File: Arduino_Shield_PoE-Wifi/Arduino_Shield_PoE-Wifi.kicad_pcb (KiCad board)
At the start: 2 copper layers, 100 x 54 mm, 83 parts, among them J1 Conn_02x08, J1 PINHD_2x4_Male, J2 Conn_02x08, J3 PINHD_1x2_Female, J4 PINHD_1x2_Female, SW1 Push_Button, T1 PMV48XP_215, U1 W5500, U2 74HC245, U2 ATECC508A-SSHDA, U3 LMV358IDGK, X2 25MHz 18pF

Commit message: Update
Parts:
- removed A1: ATWINC1500-MR210PB, Wifi_ATWINC1500-MR210PB-ND_Microchip:XCVR_ATWINC1500-MR210PB
- removed C10: 1nF 2KV 1206, PCM_4ms_Capacitor:C_1206
- removed C12, C13: 100nF_0603_16V, PCM_4ms_Capacitor:C_0603
- removed the J1 at (160.8, 137.4)
- removed LED_PB7: Yellow 0805, LED_SMD:LED_0805_2012Metric
- removed RN35, RN36: 1K_0603, PCM_Resistor_SMD_AKL:R_0603_1608Metric
- removed RN53, RN54: 10K_0603, PCM_Resistor_SMD_AKL:R_0603_1608Metric
- removed T1: PMV48XP_215, MOSFET_PMV48XP,215_Nexperia:TO-236_SOT23_NEX
- removed the U2 at (107.6, 167.3)
- removed the U2 at (190.5, 147.7)
- added C7: 10nF_0603_16V, PCM_4ms_Capacitor:C_0603, F.Cu at (200.5, 93.5)
- added C8: 1nF 2KV 1206, PCM_4ms_Capacitor:C_1206, F.Cu at (207.6, 110.0)
- added Cp3: 10uF_25V, Capacitor_THT:CP_Radial_D5.0mm_P2.00mm, F.Cu at (184.2, 139.6)
- added JP1: SolderJumper_2_Open, Connector_PinHeader_2.54mm:PinHeader_1x02_P2.54mm_Vertical, F.Cu at (152.3, 114.2)
- added JP2: SolderJumper_2_Open, Connector_PinHeader_2.54mm:PinHeader_1x02_P2.54mm_Vertical, F.Cu at (156.9, 114.2)
- added JP3: SolderJumper_2_Open, Connector_PinHeader_2.54mm:PinHeader_1x02_P2.54mm_Vertical, F.Cu at (161.6, 114.2)
- added JP4: SolderJumper_2_Open, Connector_PinHeader_2.54mm:PinHeader_1x02_P2.54mm_Vertical, F.Cu at (166.2, 114.2)
- added JP5: SolderJumper_2_Open, Connector_PinHeader_2.54mm:PinHeader_1x02_P2.54mm_Vertical, F.Cu at (170.9, 114.2)
- added JP6: SolderJumper_2_Open, Connector_PinHeader_2.54mm:PinHeader_1x02_P2.54mm_Vertical, F.Cu at (175.5, 114.2)
- added L2: MPZ1608S101ATAH0, FerriteBead_MPZ1608S101ATAH0_TDK:IND_1608_TDK, F.Cu at (184.5, 146.5)
- added LED_ACT1: LED_0805_Green, PCM_LED_SMD_AKL:LED_0805_2012Metric, F.Cu at (166.1, 121.0)
- added LED_ERR1: LED_0805_Red, PCM_LED_SMD_AKL:LED_0805_2012Metric, F.Cu at (166.1, 124.7)
- added LED_WIFI1: LED_0805_Yellow, PCM_LED_SMD_AKL:LED_0805_2012Metric, F.Cu at (166.1, 128.4)
- added ON2: LED_0805_Green, PCM_LED_SMD_AKL:LED_0805_2012Metric, F.Cu at (195.0, 145.6)
- added RG81: 1K_0603, PCM_Resistor_SMD_AKL:R_0603_1608Metric, F.Cu at (177.8, 93.5)
- added RG82: 1K_0603, PCM_Resistor_SMD_AKL:R_0603_1608Metric, F.Cu at (177.8, 96.3)
- added RG83: 1K_0603, PCM_Resistor_SMD_AKL:R_0603_1608Metric, F.Cu at (177.8, 99.0)
- added RG84: 1K_0603, PCM_Resistor_SMD_AKL:R_0603_1608Metric, F.Cu at (177.8, 101.7)
- added RG85: 1K_0603, PCM_Resistor_SMD_AKL:R_0603_1608Metric, F.Cu at (177.8, 104.4)
- added RG86: 1K_0603, PCM_Resistor_SMD_AKL:R_0603_1608Metric, F.Cu at (177.8, 107.1)
- added RG87: 1K_0603, PCM_Resistor_SMD_AKL:R_0603_1608Metric, F.Cu at (177.8, 109.9)
- added RON1: 1K_0603, PCM_Resistor_SMD_AKL:R_0603_1608Metric, F.Cu at (190.6, 140.4)
- added RON2: 1K_0603, PCM_Resistor_SMD_AKL:R_0603_1608Metric, F.Cu at (190.6, 143.2)
- added U2: ATWINC1500-MR210PA, Wifi_ATWINC1500-MR210PA_Microchip:ATWINC1500MR210PA, F.Cu at (163.3, 102.0)
- added UP1: LM7805MP, PCM_Package_TO_SOT_SMD_AKL:SOT-223-3_TabPin2, F.Cu at (197.8, 127.4)
- C1: value 10nF_0603_16V -> 100nF_0603_16V
- Cp1, Cp2: value 47uF_10V -> 10uF_25V; footprint Capacitor_THT:CP_Radial_D4.0mm_P1.50mm -> Capacitor_THT:CP_Radial_D5.0mm_P2.00mm
- L1: value MH2029-300Y -> MPZ1608S101ATAH0; footprint FerriteBead_MH2029-300Y_Bourns:IND_BOURNS_MH2029 -> FerriteBead_MPZ1608S101ATAH0_TDK:IND_1608_TDK
- ON1: value Green 0805 -> LED_0805_Green; footprint LED_SMD:LED_0805_2012Metric -> PCM_LED_SMD_AKL:LED_0805_2012Metric
- U3: value LMV358IDGK -> 74HC245; footprint PCM_Package_SO_AKL:MSOP-8_3x3mm_P0.65mm -> PCM_Package_SO_AKL:SOIC-20W_7.5x12.8mm_P1.27mm
- UP2: value LP2985-3.3 -> AMS1117-3.3; footprint Package_TO_SOT_SMD:SOT-23-5 -> Package_TO_SOT_SMD:SOT-223-3_TabPin2
- moved ON1 146.8 mm to (195.0, 141.9)
- moved UP2 135.7 mm to (197.7, 135.9)
- moved C2 123.7 mm to (190.6, 127.2)
- moved Cp2 122.6 mm to (184.2, 133.0)
- moved C3 121.2 mm to (190.6, 129.8)
- moved C4 121.2 mm to (190.6, 132.5)
- moved C5 121.2 mm to (190.6, 135.1)
- moved C6 121.2 mm to (190.6, 137.8)
- moved UP3 120.3 mm to (199.8, 142.5)
- moved Cp1 115.7 mm to (184.2, 126.5)
- moved U3 105.3 mm to (156.9, 126.4)
- moved C21 67.8 mm to (200.5, 106.8)
- moved C24 67.8 mm to (204.7, 93.5)
- moved C32 67.8 mm to (204.7, 106.8)
- moved C33 67.8 mm to (209.0, 93.5)
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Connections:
- net /PB7 renamed /Wifi/MISO_5V
- C1 pad 1: GND -> +3V3A
- C1 pad 2: Net-(C1-Pad2) -> GND
- C16 pad 1: GND -> GNDA
- C19 pad 1: GND -> GNDA
- C2 pad 1: VIN -> +3V3B
- C20 pad 2: GND -> GNDA
- C21 pad 2: GND -> GNDA
- C24 pad 2: GND -> GNDA
- C25 pad 2: GND -> GNDA
- C28 pad 2: GND -> GNDA
- C29 pad 2: GND -> GNDA
- C3 pad 1: +5V -> Net-(UP2-VO)
- C30 pad 2: GND -> GNDA
- C31 pad 1: +3V3D -> +3V3B
- C31 pad 2: GND -> GNDB
- C32 pad 1: +3V3D -> +3V3B
- C32 pad 2: GND -> GNDB
- C33 pad 2: GND -> GNDB
- C34 pad 2: GND -> GNDB
- C35 pad 1: GND -> GNDB
- C36 pad 2: GND -> GNDB
- C4 pad 1: +3V3_2 -> +3V3C
- C5 pad 1: +3V3_2 -> +3V3C
- C6 pad 1: +3V3_2 -> +3V3C
- L1 pad 1: unconnected-(L1-Pad1) -> Net-(UP2-VO)
- L1 pad 2: unconnected-(L1-Pad2) -> +3V3A
- R24 pad 2: Net-(C1-Pad2) -> Net-(C7-Pad2)
- R46 pad 2: GND -> GNDB
- R8 pad 1: /PowerOverEthernet/DUP_LED -> /PowerOverEthernet/LINK_LED
- RJ45 pad 10: GND -> GNDPWR
- RJ45 pad 11: +3V3D -> +3V3B
- RJ45 pad 13: +3V3D -> +3V3B
- RJ45 pad 7: Net-(C1-Pad2) -> Net-(C7-Pad2)
- RN21 pad 2: GND -> GNDB
- RN22 pad 2: GND -> GNDB
- RN23 pad 2: GND -> GNDB
- RN24 pad 2: GND -> GNDB
- RN31 pad 1: +3V3D -> +3V3B
- RN32 pad 1: +3V3D -> +3V3B
- RN33 pad 1: +3V3D -> +3V3B
- RN34 pad 1: +3V3D -> +3V3B
- RN41 pad 2: GND -> GNDB
- RN42 pad 2: GND -> GNDB
- RN44 pad 1: +3V3D -> +3V3B
- U1 pad 14: GND -> GNDB
- U1 pad 16: GND -> GNDB
- U1 pad 19: GND -> GNDB
- U1 pad 25: /PowerOverEthernet/DUP_LED -> /PowerOverEthernet/LINK_LED
- U1 pad 28: +3V3D -> +3V3B
- U1 pad 29: GND -> GNDB
- U1 pad 3: GND -> GNDB
- U1 pad 48: GND -> GNDB
- U1 pad 9: GND -> GNDB
- U3 pad 1: Net-(U3A--) -> +3V3C
- U3 pad 2: Net-(U3A--) -> /Wifi/CFG_5V
- U3 pad 4: GND -> /Wifi/MOSI_5V
- U3 pad 5: /Power/CMP -> /Wifi/CS_5V
- U3 pad 6: +3V3_1 -> /Wifi/EN_5V
- U3 pad 7: /Power/GATE_CMD -> /Wifi/RST_5V
- U3 pad 8: +5V -> /Wifi/SCK_5V
- UP2 pad 1: +5V -> GND
- UP2 pad 2: GND -> Net-(UP2-VO)
- UP3 pad 5: +3V3_2 -> +3V3C

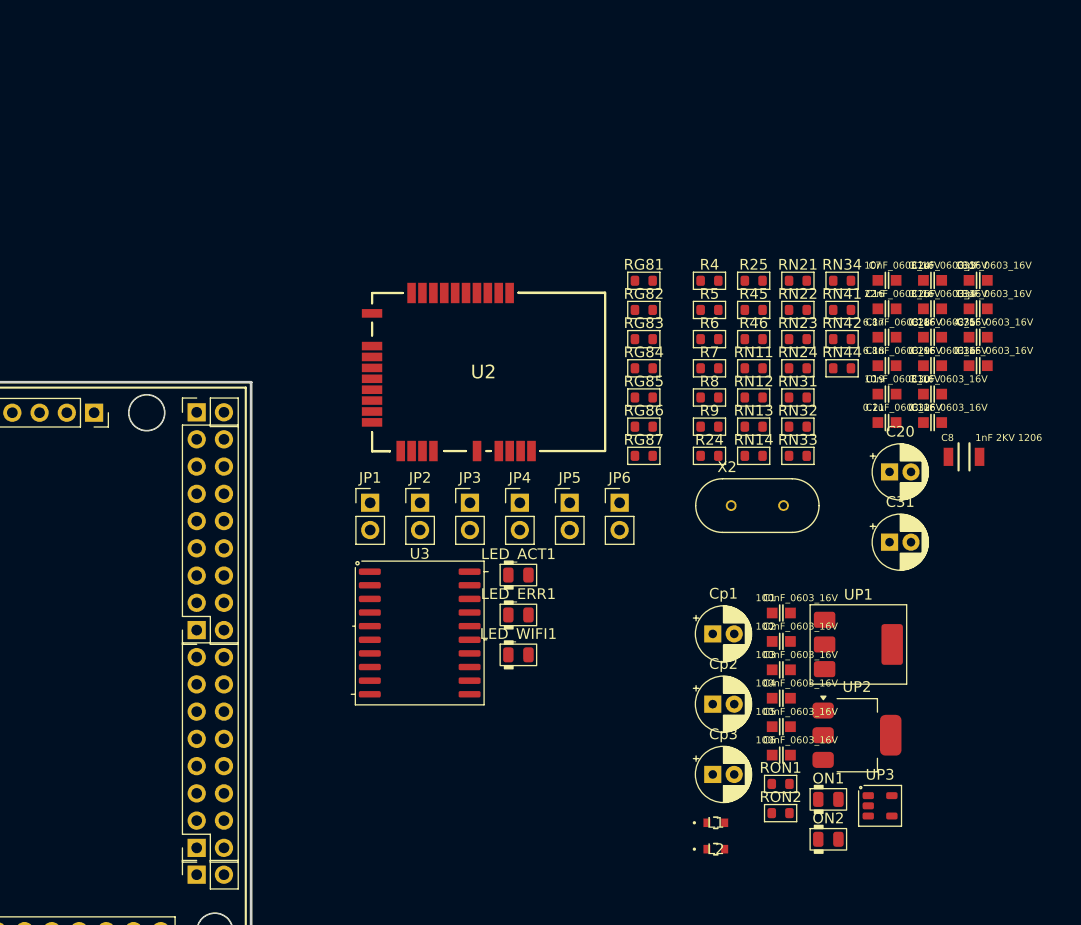
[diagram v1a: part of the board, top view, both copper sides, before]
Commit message: fixing schematics
Fix using ESP8266 12-E
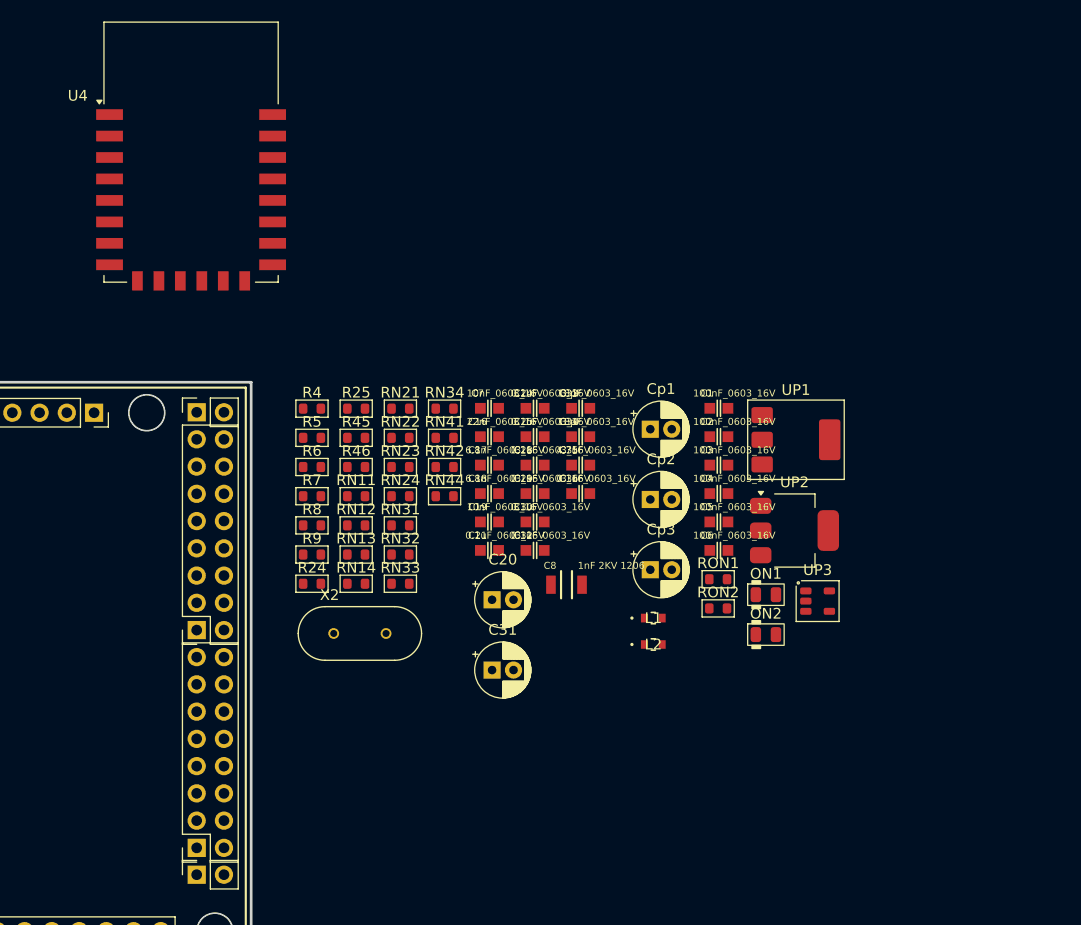
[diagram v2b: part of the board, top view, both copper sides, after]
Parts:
- removed JP1, JP2, JP3, JP4, JP5, JP6: SolderJumper_2_Open, Connector_PinHeader_2.54mm:PinHeader_1x02_P2.54mm_Vertical
- removed LED_ACT1: LED_0805_Green, PCM_LED_SMD_AKL:LED_0805_2012Metric
- removed LED_ERR1: LED_0805_Red, PCM_LED_SMD_AKL:LED_0805_2012Metric
- removed LED_WIFI1: LED_0805_Yellow, PCM_LED_SMD_AKL:LED_0805_2012Metric
- removed RG81, RG82, RG83, RG84, RG85, RG86, RG87: 1K_0603, PCM_Resistor_SMD_AKL:R_0603_1608Metric
- removed U2: ATWINC1500-MR210PA, Wifi_ATWINC1500-MR210PA_Microchip:ATWINC1500MR210PA
- removed U3: 74HC245, PCM_Package_SO_AKL:SOIC-20W_7.5x12.8mm_P1.27mm
- added U4: ESP-12E, RF_Module:ESP-12E, F.Cu at (135.6, 81.5)
- moved C16 38.9 mm to (163.4, 108.1)
- moved C17 38.9 mm to (163.4, 110.7)
- moved C18 38.9 mm to (163.4, 113.4)
- moved C19 38.9 mm to (163.4, 116.0)
- moved C20 38.9 mm to (163.7, 123.3)
- moved C21 38.9 mm to (163.4, 118.7)
- moved C24 38.9 mm to (167.7, 105.4)
- moved C25 38.9 mm to (167.7, 108.1)
- moved C28 38.9 mm to (167.7, 110.7)
- moved C29 38.9 mm to (167.7, 113.4)
- moved C30 38.9 mm to (167.7, 116.0)
- moved C31 38.9 mm to (163.7, 129.8)
- moved C32 38.9 mm to (167.7, 118.7)
- moved C33 38.9 mm to (171.9, 105.4)
- moved C34 38.9 mm to (171.9, 108.1)
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
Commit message: Update fix schematics
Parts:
- removed the UP1 at (75.2, 141.4)
- added ICSP1: ICSP_Connector_Female, Connector_PinSocket_2.54mm:PinSocket_2x03_P2.54mm_Vertical, B.Cu at (120.8, 111.5)
- added L_DUP1: LED_0805_RED, PCM_LED_SMD_AKL:LED_0805_2012Metric, F.Cu at (109.0, 78.9)
- added L_SPD1: LED_0805_RED, PCM_LED_SMD_AKL:LED_0805_2012Metric, F.Cu at (109.0, 82.7)
- added ON3: LED_0805_Green, PCM_LED_SMD_AKL:LED_0805_2012Metric, F.Cu at (88.9, 142.6)
- added RON3: 1K_0603, PCM_Resistor_SMD_AKL:R_0603_1608Metric, F.Cu at (88.7, 145.8)
- added RW1: 10K_0603, PCM_Resistor_SMD_AKL:R_0603_1608Metric, F.Cu at (108.2, 133.7)
- added RW2: 10K_0603, PCM_Resistor_SMD_AKL:R_0603_1608Metric, F.Cu at (129.7, 143.6)
- added R_DUP1: 1K_0603, PCM_Resistor_SMD_AKL:R_0603_1608Metric, F.Cu at (113.3, 78.4)
- added R_SPD1: 1K_0603, PCM_Resistor_SMD_AKL:R_0603_1608Metric, F.Cu at (113.3, 81.2)
- moved UP1 151.1 mm to (46.9, 150.5), turned to -90 degrees
- moved UP2 138.7 mm to (55.3, 140.9), turned to 180 degrees
- moved Cp2 135.3 mm to (45.9, 141.7)
- moved Cp1 128.8 mm to (56.5, 149.0), turned to 90 degrees
- moved ON1 125.3 mm to (66.1, 146.4), turned to -90 degrees
- moved C8 124.7 mm to (46.9, 137.3)
- moved UP3 124.2 mm to (71.6, 144.4)
- moved ON2 124.1 mm to (66.1, 142.6), turned to -90 degrees
- moved RON1 123.9 mm to (63.4, 146.5), turned to 90 degrees
- moved RON2 122.7 mm to (63.4, 142.6), turned to 90 degrees
- moved Cp3 117.3 mm to (62.3, 137.7)
- moved C1 116.6 mm to (72.4, 136.6)
- moved C2 116.6 mm to (72.4, 139.0)
- moved C4 113.9 mm to (75.2, 144.4), turned to -90 degrees
- moved C5 111.1 mm to (77.4, 144.4), turned to -90 degrees
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- renumbered U4 to U2
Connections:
- net EARTH renamed Earth
- C16 pad 1: GNDA -> GND
- C19 pad 1: GNDA -> GND
- C20 pad 2: GNDA -> GND
- C21 pad 2: GNDA -> GND
- C24 pad 2: GNDA -> GND
- C25 pad 2: GNDA -> GND
- C28 pad 2: GNDA -> GND
- C29 pad 2: GNDA -> GND
- C30 pad 2: GNDA -> GND
- C31 pad 2: GNDB -> GND
- C32 pad 2: GNDB -> GND
- C33 pad 2: GNDB -> GND
- C34 pad 2: GNDB -> GND
- C35 pad 1: GNDB -> GND
- C36 pad 2: GNDB -> GND
- C7 pad 1: GNDA -> GND
- C8 pad 1: GNDA -> GND
- PWM1 pad 5: /PG5 -> unconnected-(PWM1-Pad5)
- PWM1 pad 7: /PH3 -> unconnected-(PWM1-Pad7)
- PWM1 pad 8: /PH4 -> unconnected-(PWM1-Pad8)
- PWM2 pad 1: /PH5 -> unconnected-(PWM2-Pad1)
- PWM2 pad 2: /PH6 -> unconnected-(PWM2-Pad2)
- PWM2 pad 8: /AREF -> unconnected-(PWM2-Pad8)
- PWR1 pad 8: +12V -> VIN
- R46 pad 2: GNDB -> GND
- RJ45 pad 10: GNDPWR -> GND
- RJ45 pad 9: +12V -> VIN
- RN21 pad 2: GNDB -> GND
- RN22 pad 2: GNDB -> GND
- RN23 pad 2: GNDB -> GND
- RN24 pad 2: GNDB -> GND
- RN41 pad 2: GNDB -> GND
- RN42 pad 2: GNDB -> GND
- U1 pad 14: GNDB -> GND
- U1 pad 16: GNDB -> GND
- U1 pad 19: GNDB -> GND
- U1 pad 29: GNDB -> GND
- U1 pad 3: GNDB -> GND
- U1 pad 33: /PowerOverEthernet/SCK_ETH -> /PB1
- U1 pad 34: /PowerOverEthernet/MISO_ETH -> /PB3
- U1 pad 35: /PowerOverEthernet/MOSI_ETH -> /PB2
- U1 pad 37: /PowerOverEthernet/RESET_ETH -> /RESET1
- U1 pad 48: GNDB -> GND
- U1 pad 9: GNDB -> GND
- U2 pad 1: unconnected-(U4-~{RST}-Pad1) -> /RESET1
- U2 pad 15: unconnected-(U4-GND-Pad15) -> GND
- U2 pad 16: unconnected-(U4-GPIO15-Pad16) -> Net-(U2-GPIO15)
- U2 pad 18: unconnected-(U4-GPIO0-Pad18) -> /Wifi ESP8266_12-E/FLASH
- U2 pad 2: unconnected-(U4-ADC-Pad2) -> Net-(U2-ADC)
- U2 pad 21: unconnected-(U4-GPIO3/RXD-Pad21) -> /RXD1
- U2 pad 22: unconnected-(U4-GPIO1/TXD-Pad22) -> /TXD1
- U2 pad 8: unconnected-(U4-VCC-Pad8) -> +3V3C
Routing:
- net GND: track 0.00 -> 191.3 mm, vias 0 -> 6
- net +5V: track 0.00 -> 73.2 mm, vias 0 -> 4
- net VIN: track 0.00 -> 36.6 mm
- net Net-(UP2-VO): track 0.00 -> 27.9 mm, vias 0 -> 1
- net Earth: track 0.00 -> 22.8 mm
- net +3V3B: track 0.00 -> 14.6 mm
- net +3V3C: track 0.00 -> 6.84 mm
- net Net-(ON2-A): track 0.00 -> 2.75 mm
- net Net-(ON1-A): track 0.00 -> 2.71 mm
- net +3V3A: track 0.00 -> 1.92 mm

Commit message: Update
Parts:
- moved C20 95.2 mm to (68.6, 128.4)
- moved C21 95.2 mm to (68.4, 123.8)
- moved C24 95.2 mm to (72.6, 110.5)
- moved C25 95.2 mm to (72.6, 113.2)
- moved C28 95.2 mm to (72.6, 115.8)
- moved C29 95.2 mm to (72.6, 118.5)
- moved C30 95.2 mm to (72.6, 121.2)
- moved RN34 54.1 mm to (97.2, 129.8), turned to 90 degrees
- moved R45 53.0 mm to (88.7, 142.4), turned to 180 degrees
- moved C33 50.4 mm to (92.2, 142.4)
- moved RN44 46.3 mm to (99.7, 130.0), turned to 90 degrees
- moved C34 46.2 mm to (85.2, 142.4), turned to 180 degrees
- moved X2 44.3 mm to (88.7, 138.4)
- moved RN31 43.1 mm to (89.5, 129.7), turned to 90 degrees
- moved RN32 40.4 mm to (92.2, 129.7), turned to 90 degrees
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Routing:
- net Net-(R9-Pad2): track 0.00 -> 33.6 mm, vias 0 -> 1
- net Net-(R8-Pad2): track 0.00 -> 19.9 mm, vias 0 -> 1
- net /PowerOverEthernet/TCT: track 0.00 -> 19.5 mm, vias 0 -> 1
- net GND: track 191.3 -> 201.9 mm
- net Net-(C7-Pad2): track 0.00 -> 8.24 mm, vias 0 -> 1
- net /RESET1: track 0.00 -> 6.50 mm
- net Net-(U1-XI/CLKIN): track 0.00 -> 5.91 mm
- net Net-(U1-XO): track 0.00 -> 5.91 mm
- net Net-(ON3-A): track 0.00 -> 2.70 mm
- net +3V3A: track 1.92 -> 3.96 mm
- net +3V3C: track 6.84 -> 8.67 mm

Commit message: Update
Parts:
- moved R4 28.7 mm to (63.3, 111.8), turned to 90 degrees
- moved R5 26.3 mm to (66.0, 111.8), turned to 90 degrees
- moved R6 24.3 mm to (68.7, 111.8), turned to 90 degrees
- moved RN14 22.9 mm to (73.2, 129.4), turned to 180 degrees
- moved R7 22.7 mm to (71.5, 111.8), turned to 90 degrees
- moved C19 21.0 mm to (73.9, 112.4), turned to 90 degrees
- moved RN13 19.6 mm to (73.2, 127.4), turned to 180 degrees
- moved RN34 19.2 mm to (81.2, 119.2), turned to -90 degrees
- moved RN33 18.9 mm to (79.2, 119.2), turned to -90 degrees
- moved C33 18.6 mm to (95.6, 124.1), turned to 90 degrees
- moved RN32 18.3 mm to (77.2, 119.2), turned to -90 degrees
- moved RN12 16.3 mm to (73.2, 125.4), turned to 180 degrees
- moved R45 16.3 mm to (95.6, 127.6), turned to -90 degrees
- moved C24 16.0 mm to (68.1, 125.9)
- moved C34 15.4 mm to (95.6, 131.1), turned to -90 degrees
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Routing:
- net GND: track 201.9 -> 276.4 mm
- net +3V3A: track 3.96 -> 60.3 mm, vias 0 -> 5
- net +3V3B: track 14.6 -> 67.5 mm, vias 0 -> 1
- net Net-(U1-XI/CLKIN): track 5.91 -> 13.6 mm
- net Net-(U1-XO): track 5.91 -> 13.2 mm
- net Net-(U1-PMODE0): track 0.00 -> 6.40 mm
- net /PowerOverEthernet/RXP1: track 0.00 -> 5.58 mm
- net Net-(U1-PMODE1): track 0.00 -> 4.72 mm
- net /PowerOverEthernet/TXN1: track 0.00 -> 4.23 mm
- net /PowerOverEthernet/RXN1: track 0.00 -> 4.02 mm
- net /PowerOverEthernet/TXP1: track 0.00 -> 3.82 mm
- net Net-(U1-PMODE2): track 0.00 -> 3.40 mm

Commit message: Update
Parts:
- moved R_DUP1 64.5 mm to (91.0, 139.0)
- moved L_DUP1 63.8 mm to (87.4, 139.0)
- moved R_SPD1 58.3 mm to (91.0, 135.0)
- moved C3 57.0 mm to (63.2, 133.0)
- moved L_SPD1 56.6 mm to (87.4, 135.0)
- moved R9 45.6 mm to (91.0, 141.0)
- moved C18 44.9 mm to (63.1, 119.4)
- moved C17 44.6 mm to (63.1, 121.4)
- moved R8 41.8 mm to (91.0, 137.0)
- moved R46 25.6 mm to (78.9, 125.9), turned to 180 degrees
- moved RN24 18.2 mm to (85.0, 111.4), turned to 90 degrees
- moved C35 18.0 mm to (90.7, 131.1), turned to 90 degrees
- moved RW2 16.9 mm to (122.6, 128.2), turned to 0 degrees
- moved RW1 16.2 mm to (112.5, 149.3), turned to 180 degrees
- moved C19 15.7 mm to (71.7, 127.9), turned to 180 degrees
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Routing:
- net GND: track 276.4 -> 496.1 mm, vias 6 -> 17
- net /RESET1: track 6.50 -> 185.9 mm, vias 0 -> 3
- net +5V: track 73.2 -> 188.8 mm, vias 4 -> 7
- net +3V3B: track 67.5 -> 158.2 mm, vias 1 -> 6
- net /PB1: track 0.00 -> 81.9 mm, vias 0 -> 4
- net /PB3: track 0.00 -> 78.4 mm, vias 0 -> 3
- net /PB2: track 0.00 -> 73.1 mm, vias 0 -> 4
- net Net-(R9-Pad2): track 33.6 -> 94.0 mm
- net Net-(R8-Pad2): track 19.9 -> 79.2 mm
- net +3V3C: track 8.67 -> 62.6 mm, vias 0 -> 1
- net /RXD1: track 0.00 -> 33.9 mm, vias 0 -> 1
- net /PowerOverEthernet/TXN2: track 0.00 -> 33.6 mm, vias 0 -> 1
- net VIN: track 36.6 -> 69.5 mm, vias 0 -> 3
- net /TXD1: track 0.00 -> 32.9 mm, vias 0 -> 1
- net /PowerOverEthernet/TXP2: track 0.00 -> 29.6 mm, vias 0 -> 1
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
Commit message: Update
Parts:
- RJ45: footprint Connector_RJ:RJ45_Abracon_ARJP11A-MA_Horizontal -> RJ45_RJ45_Abracon_ARJP11A-MA_Horizontal-edited:RJ45_Abracon_ARJP11A-MA_Horizontal-edited
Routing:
- net +5V: track 188.8 -> 68.7 mm, vias 7 -> 5
- net /RESET1: track 185.9 -> 190.3 mm, vias 3 -> 4
- net +3V3B: track 158.2 -> 161.1 mm, vias 6 -> 5
- net Net-(RJ45-RD+): track 9.51 -> 6.93 mm
- net GND: track 496.1 -> 493.6 mm, vias 17 -> 26
- net /PowerOverEthernet/TXP2: track 29.6 -> 31.9 mm
- net /PowerOverEthernet/TXN2: track 33.6 -> 35.2 mm
- net Net-(UP2-VO): track 30.8 -> 29.2 mm, vias 0 -> 1
- net VIN: track 69.5 -> 68.0 mm, vias 3 -> 2
- net Net-(R9-Pad2): track 94.0 -> 92.8 mm
- net /PowerOverEthernet/TCT: track 19.5 -> 18.5 mm
- net /TXD1: track 32.9 -> 33.8 mm
- net +3V3C: track 62.6 -> 63.1 mm, vias 1 -> 0
